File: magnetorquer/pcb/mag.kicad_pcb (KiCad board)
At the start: 2 copper layers, 17 parts, among them J1 Conn_01x02, J2 Conn_01x02, U1 L293

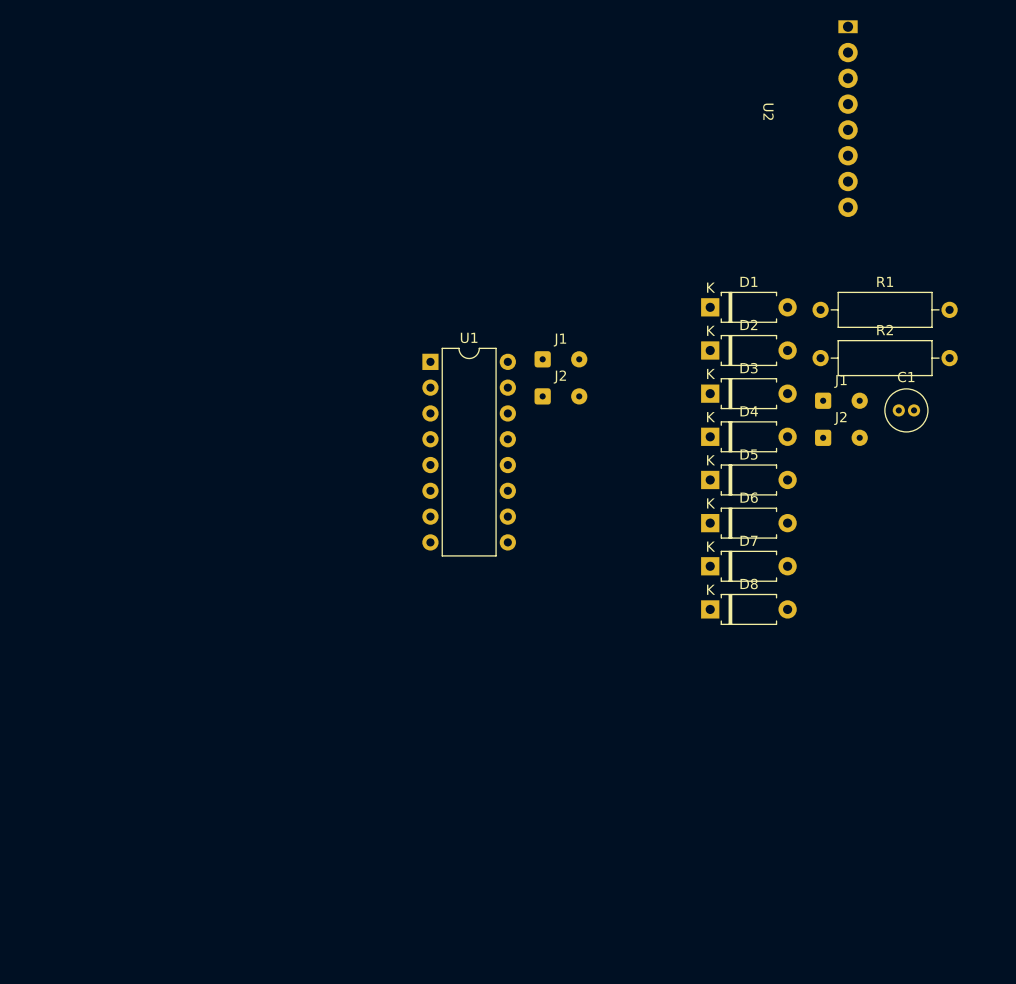
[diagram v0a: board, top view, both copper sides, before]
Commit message: feat: lilygo s3 sch/footprint clean up sch
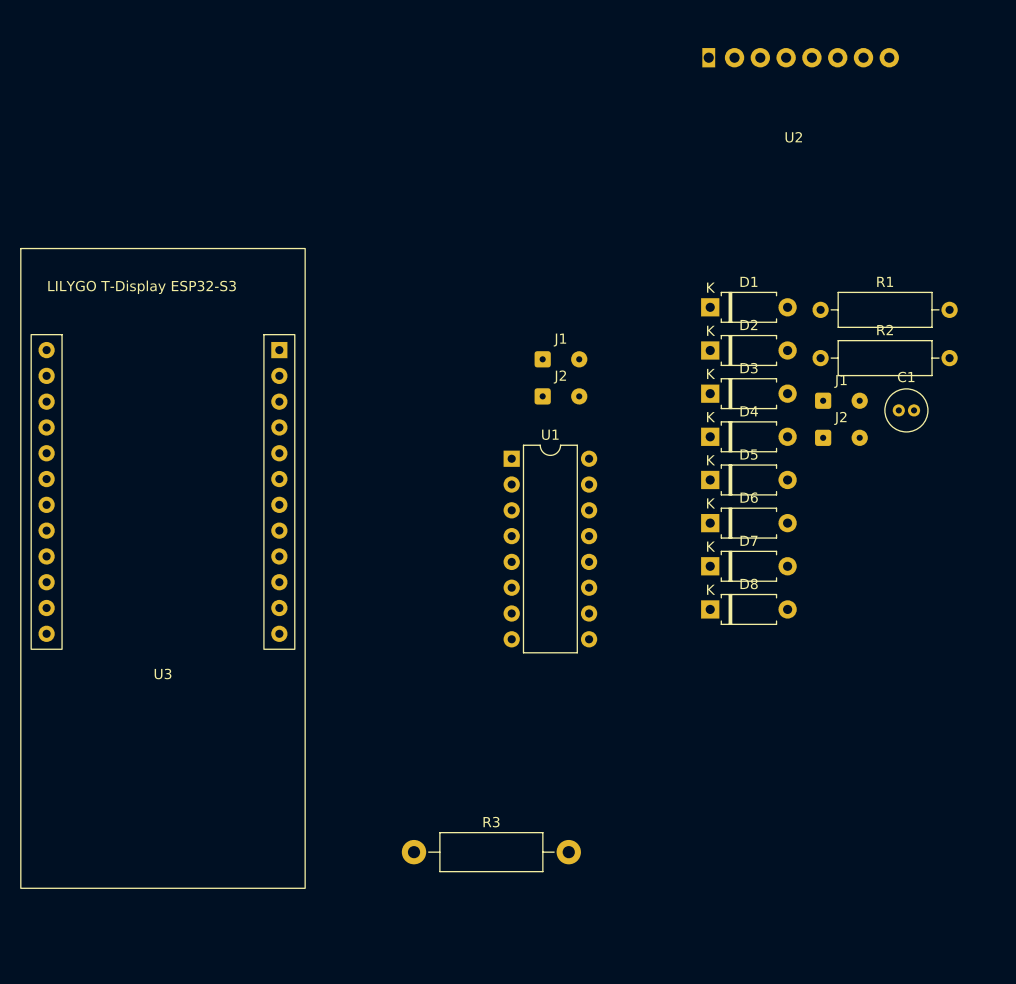
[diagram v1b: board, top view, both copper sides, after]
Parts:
- added R3: R, Resistor_THT:R_Axial_DIN0411_L9.9mm_D3.6mm_P15.24mm_Horizontal, F.Cu at (112.3, 131.5)
- added U3: ~, ESP32_boards:LILYGO_T-Display_ESP32-S3, F.Cu at (87.5, 72.1)
- moved U1 12.5 mm to (121.9, 92.8)
- turned U2 to 90 degrees
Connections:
- U2 pad 1: unconnected-(U2-VIN-Pad1) -> +3.3V
- U2 pad 3: unconnected-(U2-GND-Pad3) -> GND
- U2 pad 4: unconnected-(U2-SCL-Pad4) -> /MPU-9255/SCL
- U2 pad 5: unconnected-(U2-SDA-Pad5) -> /MPU-9255/SDA
- U2 pad 6: unconnected-(U2-AD0-Pad6) -> /MPU-9255/AD0

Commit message: feat: upload all changes for sch
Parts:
- removed the J1 at (124.9, 83.0)
- removed the J1 at (152.6, 87.0)
- removed the J2 at (124.9, 86.6)
- removed the J2 at (152.6, 90.7)
- removed R3: R, Resistor_THT:R_Axial_DIN0411_L9.9mm_D3.6mm_P15.24mm_Horizontal
- added J1: Conn_01x02, Connector_Wire:SolderWire-0.1sqmm_1x02_P3.6mm_D0.4mm_OD1mm, F.Cu at (144.1, 68.2)
- added J2: Conn_01x02, Connector_Wire:SolderWire-0.1sqmm_1x02_P3.6mm_D0.4mm_OD1mm, F.Cu at (144.1, 71.9)
- added J3: Conn_01x03, Connector_PinHeader_2.54mm:PinHeader_1x03_P2.54mm_Vertical, F.Cu at (146.5, 104.7)
- added J4: Conn_01x03, Connector_PinHeader_2.54mm:PinHeader_1x03_P2.54mm_Vertical, F.Cu at (139.8, 104.7)
- added J5: Conn_01x03, Connector_PinHeader_2.54mm:PinHeader_1x03_P2.54mm_Vertical, F.Cu at (139.8, 116.4)
- added J6: Conn_01x03, Connector_PinHeader_2.54mm:PinHeader_1x03_P2.54mm_Vertical, F.Cu at (146.5, 116.4)
- moved U2 58.1 mm to (128.1, 112.6), turned to 0 degrees
- moved U1 26.7 mm to (133.1, 68.5)
- moved R1 23.0 mm to (133.0, 90.7)
- moved R2 23.0 mm to (133.0, 95.4)
- moved D1 21.4 mm to (122.1, 68.5)
- moved D2 21.4 mm to (122.1, 72.8)
- moved D3 21.4 mm to (122.1, 77.0)
- moved D4 21.4 mm to (122.1, 81.3)
- moved D5 21.4 mm to (122.1, 85.5)
- moved D6 21.4 mm to (122.1, 89.8)
- moved D7 21.4 mm to (122.1, 94.0)
- moved D8 21.4 mm to (122.1, 98.3)
- moved C1 19.5 mm to (144.3, 76.5)
- moved U3 17.1 mm to (103.9, 67.1)
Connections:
- net /ESP32/LDR_2 renamed /ESP32/LDR_Back
- net /ESP32/LDR_3 renamed /ESP32/LDR_Left
- net /ESP32/LDR_4 renamed /ESP32/LDR_Right
- U2 pad 4: /MPU-9255/SCL -> /ESP32/SCL
- U2 pad 5: /MPU-9255/SDA -> /ESP32/SDA
- U3 pad 17: /ESP32/MagI2C -> /ESP32/SDA
- U3 pad 18: /ESP32/MagI2C -> /ESP32/SCL
- U3 pad 2: /ESP32/LDR_1 -> /ESP32/LDR_Forward
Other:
- board outline added: 92 x 92 mm

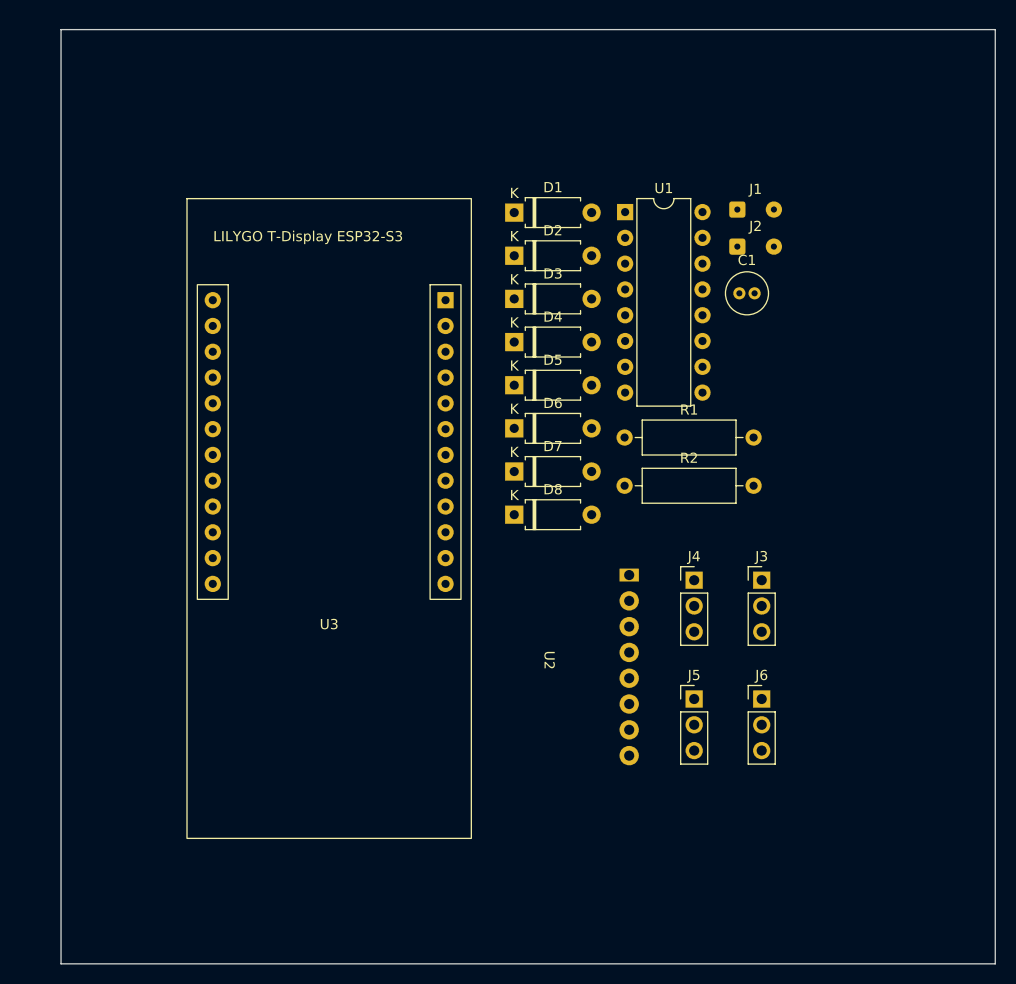
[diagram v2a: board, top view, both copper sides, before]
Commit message: start routing pcb
It needs a power regulator and a battery terminal
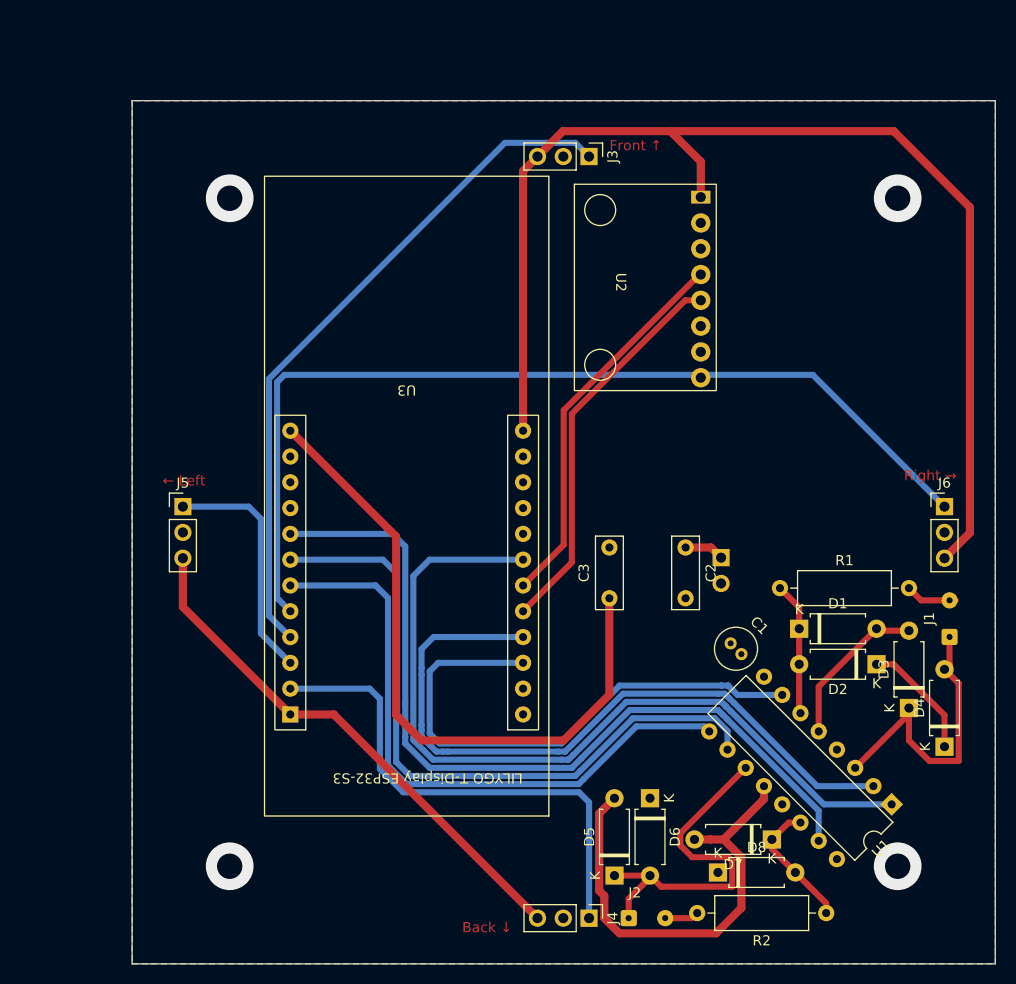
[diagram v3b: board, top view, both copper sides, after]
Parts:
- added C2: 0.22uF, Capacitor_THT:C_Rect_L7.0mm_W2.5mm_P5.00mm, F.Cu at (139.0, 101.5)
- added C3: 0.1uF, Capacitor_THT:C_Rect_L7.0mm_W2.5mm_P5.00mm, F.Cu at (131.5, 106.5)
- added J7: Conn_01x02_Pin, Connector_PinHeader_2.54mm:PinHeader_1x02_P2.54mm_Vertical, B.Cu at (142.5, 102.5)
- moved J2 67.0 mm to (133.4, 138.0)
- moved U1 64.0 mm to (159.3, 126.8), turned to -135 degrees
- moved U3 61.3 mm to (111.5, 127.9), turned to 180 degrees
- moved D4 58.2 mm to (164.5, 121.1), turned to 90 degrees
- moved D3 56.0 mm to (161.0, 117.3), turned to 90 degrees
- moved J5 53.8 mm to (89.5, 97.5)
- moved D2 53.8 mm to (157.8, 113.0), turned to 180 degrees
- moved D1 49.7 mm to (150.2, 109.5)
- moved D5 49.3 mm to (132.0, 133.8), turned to 90 degrees
- moved J1 47.0 mm to (165.0, 110.3), turned to 90 degrees
- moved R2 46.5 mm to (152.8, 137.5), turned to 180 degrees
- moved J3 45.1 mm to (129.5, 63.0), turned to -90 degrees
- moved D7 44.2 mm to (147.5, 130.2), turned to 180 degrees
- moved D8 40.5 mm to (142.2, 133.5)
- moved D6 38.8 mm to (135.5, 126.2), turned to -90 degrees
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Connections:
- J3 pad 1: /LDR_Forward -> /LDR.Forward
- J4 pad 1: /LDR_Back -> /LDR.Back
- J5 pad 1: /LDR_Left -> /LDR.Left
- J6 pad 1: /LDR_Right -> /LDR.Right
- U1 pad 1: +5V -> /ACS_mag/mag1.EN
- U1 pad 10: /ACS_mag/mag2_pos -> /ACS_mag/mag2.CCW
- U1 pad 15: /ACS_mag/mag2_neg -> /ACS_mag/mag2.CW
- U1 pad 2: /ACS_mag/mag1_pos -> /ACS_mag/mag1.CCW
- U1 pad 7: /ACS_mag/mag1_neg -> /ACS_mag/mag1.CW
- U1 pad 9: +5V -> /ACS_mag/mag2.EN
- U2 pad 6: /MPU-9255/AD0 -> GND
- U3 pad 15: /ESP32/1,2EN -> /ACS_mag/mag1.CW
- U3 pad 16: /ESP32/3,4EN -> /ACS_mag/mag1.CCW
- U3 pad 19: /ESP32/1A -> /ACS_mag/mag1.EN
- U3 pad 2: /ESP32/LDR_Forward -> /LDR.Back
- U3 pad 20: /ESP32/2A -> unconnected-(U3-16-Pad20)
- U3 pad 3: /ESP32/LDR_Back -> /LDR.Left
- U3 pad 4: /ESP32/LDR_Left -> /LDR.Forward
- U3 pad 5: /ESP32/LDR_Right -> /LDR.Right
- U3 pad 6: unconnected-(U3-11-Pad6) -> /ACS_mag/mag2.EN
- U3 pad 7: /ESP32/4A -> /ACS_mag/mag2.CCW
- U3 pad 8: /ESP32/3A -> /ACS_mag/mag2.CW
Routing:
- net +3.3V: track 0.00 -> 170.1 mm
- net /LDR.Right: track 0.00 -> 94.5 mm
- net /ACS_mag/mag2.CW: track 0.00 -> 82.4 mm
- net /ACS_mag/mag1.EN: track 0.00 -> 82.1 mm
- net /ACS_mag/mag1.CCW: track 0.00 -> 70.4 mm
- net /LDR.Forward: track 0.00 -> 68.0 mm
- net /ACS_mag/mag2.CCW: track 0.00 -> 67.5 mm
- net +5V: track 0.00 -> 65.7 mm
- net /ACS_mag/mag2.EN: track 0.00 -> 61.6 mm
- net GND: track 0.00 -> 60.8 mm
- net /ACS_mag/mag1.CW: track 0.00 -> 53.5 mm
- net /LDR.Back: track 0.00 -> 49.5 mm
- net /ESP32/SDA: track 0.00 -> 38.8 mm
- net /ESP32/SCL: track 0.00 -> 37.9 mm
- net Net-(D5-K): track 0.00 -> 35.7 mm
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- added copper zone on B.Cu, net GND
- added copper zone on F.Cu, net GND
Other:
- board size 92 x 92 mm -> 85 x 85 mm
- board text added: "Back ↓"
- board text added: "Front ↑"
- board text added: "Right →"
- board text added: "← Left"

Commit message: Power reg. and v.1 print
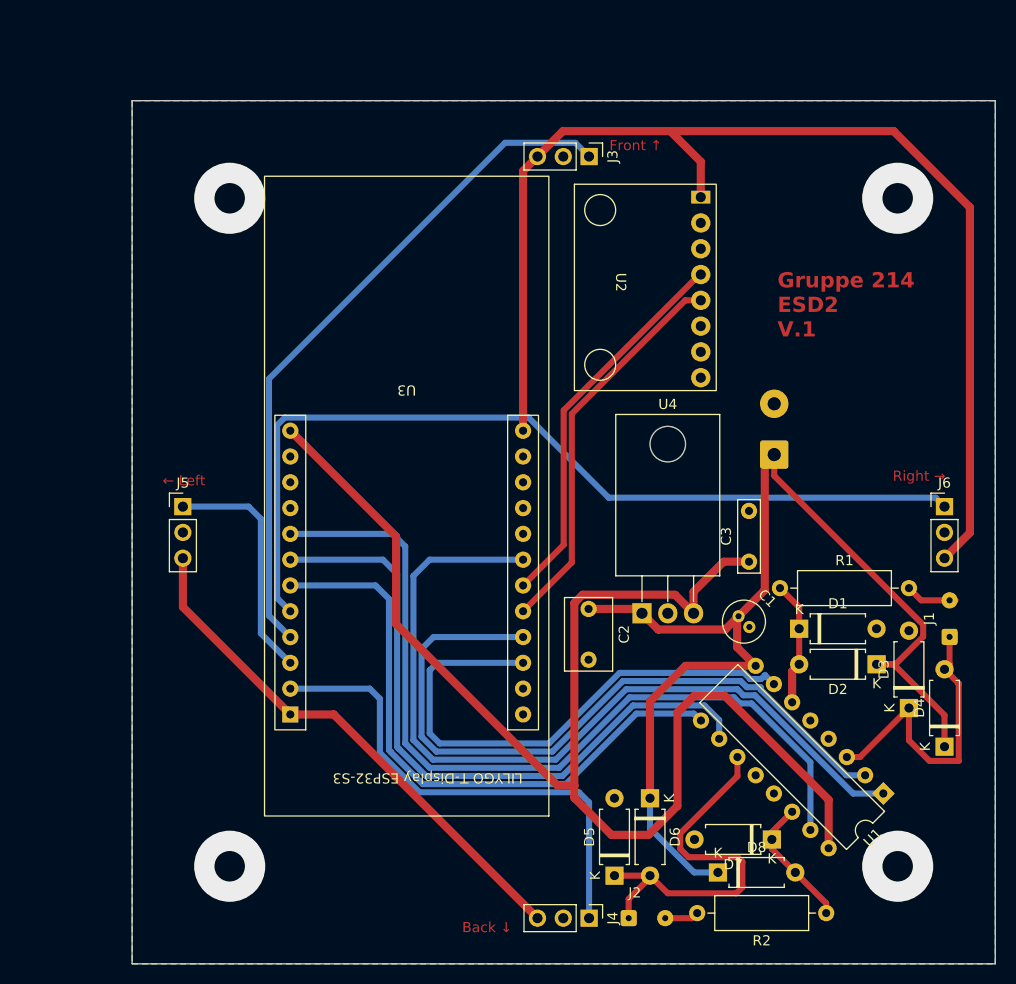
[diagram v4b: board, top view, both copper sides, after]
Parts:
- added U4: L7805, Package_TO_SOT_THT:TO-220-3_Horizontal_TabDown, F.Cu at (134.7, 108.0)
- C2: value 0.22uF -> 0.47uF; footprint Capacitor_THT:C_Rect_L7.0mm_W2.5mm_P5.00mm -> Capacitor_THT:C_Rect_L7.0mm_W4.5mm_P5.00mm
- C3: footprint Capacitor_THT:C_Rect_L7.0mm_W2.5mm_P5.00mm -> Capacitor_THT:C_Rect_L7.0mm_W2.0mm_P5.00mm
- J7: footprint Connector_PinHeader_2.54mm:PinHeader_1x02_P2.54mm_Vertical -> TerminalBlock:TerminalBlock_MaiXu_MX126-5.0-02P_1x02_P5.00mm
- moved C3 14.2 mm to (145.2, 102.9)
- moved J7 11.4 mm to (147.7, 92.3), turned to 90 degrees
- moved C2 11.3 mm to (129.4, 107.5)
- moved C1 2.78 mm to (144.2, 108.3)
- moved U1 1.35 mm to (158.5, 125.7)
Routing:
- net VCC: track 15.8 -> 113.7 mm
- net +5V: track 65.7 -> 135.0 mm
- net GND: track 60.8 -> 0.00 mm, vias 0 -> 4
- net /LDR.Right: track 94.5 -> 88.5 mm
- net Net-(D5-K): track 35.7 -> 39.2 mm
- net /ACS_mag/mag2.CW: track 82.4 -> 84.3 mm
- net /ACS_mag/mag2.EN: track 61.6 -> 60.4 mm
- net /ACS_mag/mag2.CCW: track 67.5 -> 66.4 mm
- net /LDR.Back: track 49.5 -> 48.6 mm
- net Net-(D1-K): track 13.2 -> 12.3 mm
- net Net-(D3-K): track 30.0 -> 30.6 mm
- net (no net): vias 4 -> 0
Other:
- board text added: "Gruppe 214 ESD2 V.1"
